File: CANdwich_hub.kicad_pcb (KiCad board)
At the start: 2 copper layers, 53.6 x 28 mm, 56 parts, among them J1 USB_C_Receptacle_USB2.0, J2 Conn_01x04_Socket, J3 Conn_01x04_Socket, J4 Conn_01x04_Socket, J5 Conn_01x04_Socket, U1 AP2127K-3.3, U2 USB2514B_Bi, Y1 7U24000E08UCG

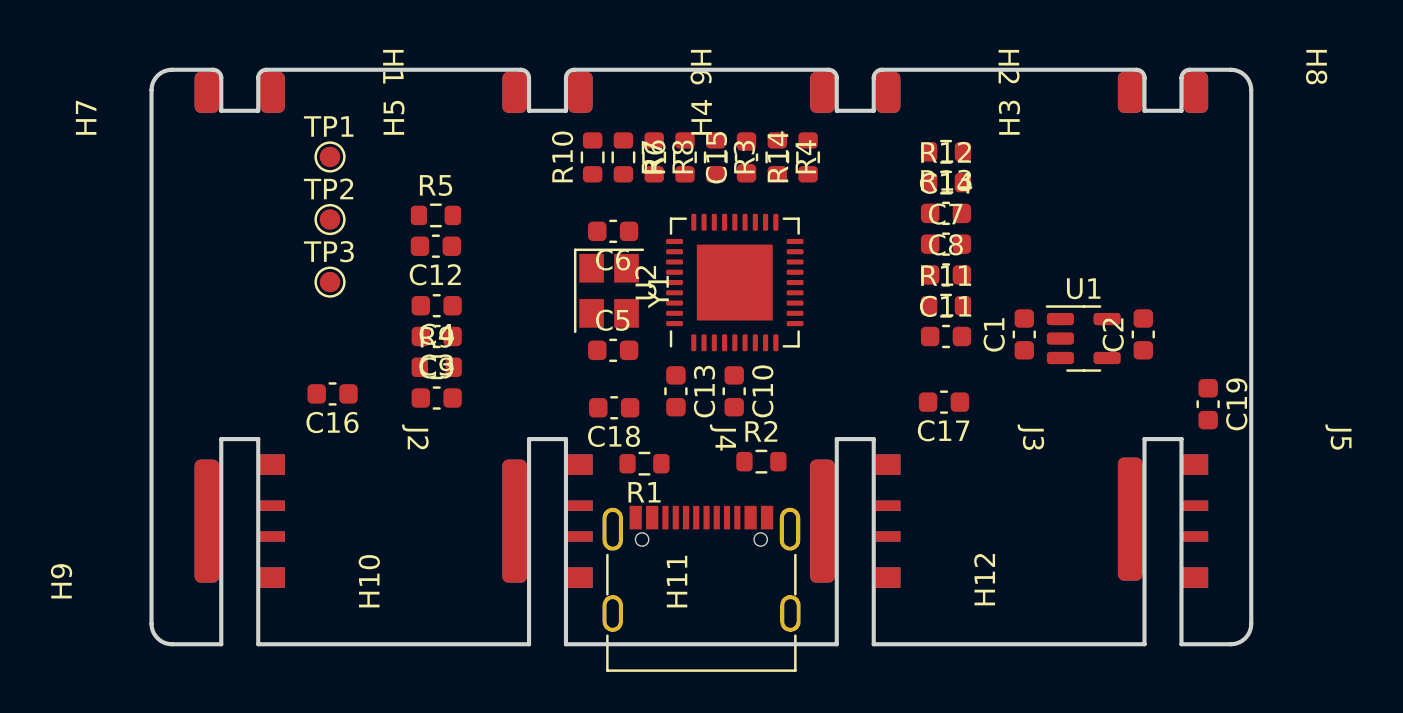
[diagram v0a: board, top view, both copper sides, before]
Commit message: Change stack up to 4 layers
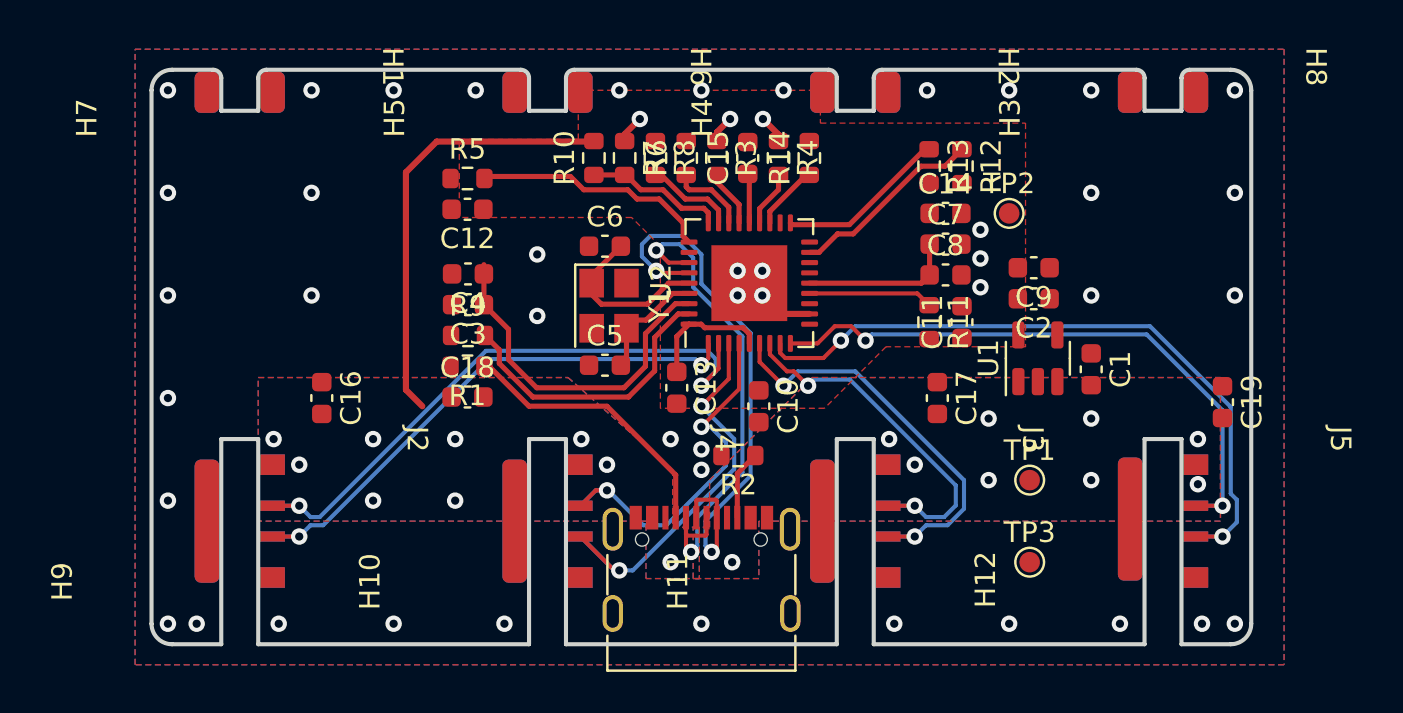
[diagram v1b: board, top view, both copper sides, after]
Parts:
- moved TP1 37.6 mm to (216.0, 122.0)
- moved TP3 36.7 mm to (216.0, 126.0)
- moved TP2 33.1 mm to (215.0, 109.0)
- moved C9 29.8 mm to (216.2, 111.7), turned to 180 degrees
- moved R1 9.85 mm to (188.6, 116.5)
- moved C18 7.17 mm to (188.6, 118.0), turned to 0 degrees
- moved C2 5.61 mm to (216.2, 113.2), turned to 180 degrees
- moved C1 3.68 mm to (219.0, 116.6), turned to -90 degrees
- moved U1 2.44 mm to (216.4, 116.1), turned to 90 degrees
- moved C12 2.37 mm to (188.6, 108.8)
- moved R5 2.37 mm to (188.6, 107.3)
- moved C3 2.17 mm to (188.6, 113.5)
- moved C4 2.17 mm to (188.6, 112.0)
- moved R9 2.17 mm to (188.6, 115.0)
- moved C10 1.40 mm to (202.8, 118.4)
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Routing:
- net /USB4_D-: track 0.00 -> 34.1 mm, vias 0 -> 2
- net /USB1_D+: track 0.00 -> 30.6 mm, vias 0 -> 2
- net /USB4_D+: track 0.00 -> 30.6 mm, vias 0 -> 2
- net /USB_D+: track 0.00 -> 27.7 mm, vias 0 -> 2
- net /USB1_D-: track 0.00 -> 27.1 mm, vias 0 -> 2
- net /USB_D-: track 0.00 -> 24.9 mm, vias 0 -> 2
- net VBUS: track 0.00 -> 21.5 mm, vias 0 -> 18
- net /USB3_D-: track 0.00 -> 20.8 mm, vias 0 -> 2
- net /USB2_D-: track 0.00 -> 20.1 mm, vias 0 -> 2
- net /USB3_D+: track 0.00 -> 18.5 mm, vias 0 -> 2
- net /USB2_D+: track 0.00 -> 18.4 mm, vias 0 -> 2
- net Net-(U2-PLLFILT): track 0.00 -> 17.1 mm
- net Net-(U2-RBIAS): track 0.00 -> 14.2 mm
- net Net-(J1-CC1): track 0.00 -> 13.6 mm
- net Net-(U2-SUSP_IND/LOCAL_PWR/NON_REM0): track 0.00 -> 11.7 mm
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- added copper zone on B.Cu, net Earth
- added copper zone on F.Cu, net Earth
- added copper zone on In1.Cu, net Earth
- added copper zone on In2.Cu, net Earth
- added copper zone on B.Cu, net VBUS
- added copper zone on F.Cu, net VBUS
- added copper zone on F.Cu, net VD3V3
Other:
- copper layers 2 -> 4
